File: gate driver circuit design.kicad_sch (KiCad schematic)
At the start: 105 parts, among them J101 90122-0763, J102 90121-0762, J103 90121-0762, Q1 CSD17313Q2, Q2 MMBT3904T-7-F, Q3 MMBT3904T-7-F, Q4 MMBT3904T-7-F, T1 750343725, T2 750343725, U1 SN6501QDBVRQ1, U2 TPS7B6950QDCYRQ1, U3 TL431AQDBZRQ1, U4 SN6501QDBVRQ1, U5 TL431AQDBZRQ1, U6 UCC21530QDWKRQ1, U7 ISO7721QDRQ1, U8 LMV762QMA_NOPB, U9 TL431AQDBZRQ1

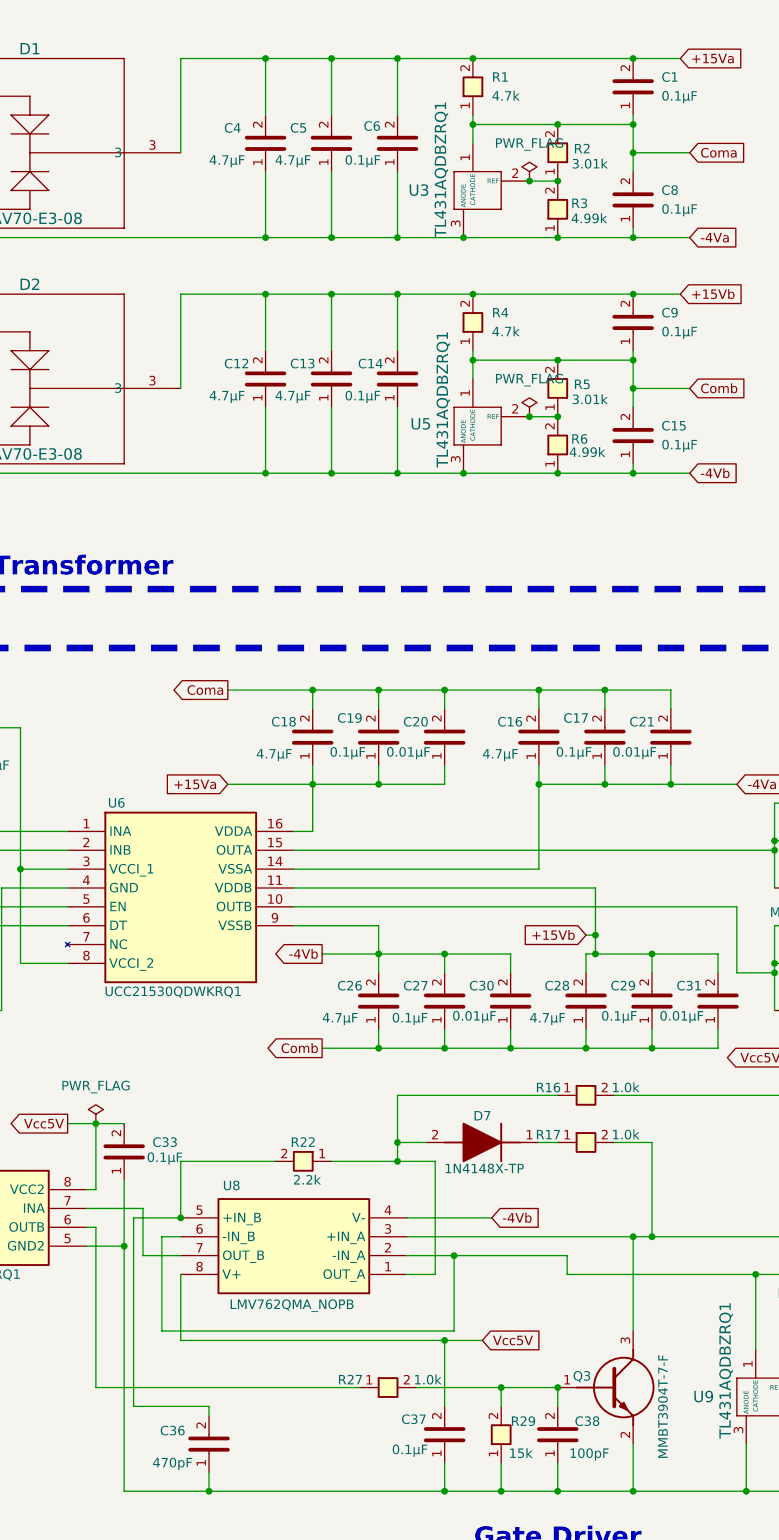
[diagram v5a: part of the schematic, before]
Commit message: Final PCB design TI gate driver
TI gate driver final PCB design files
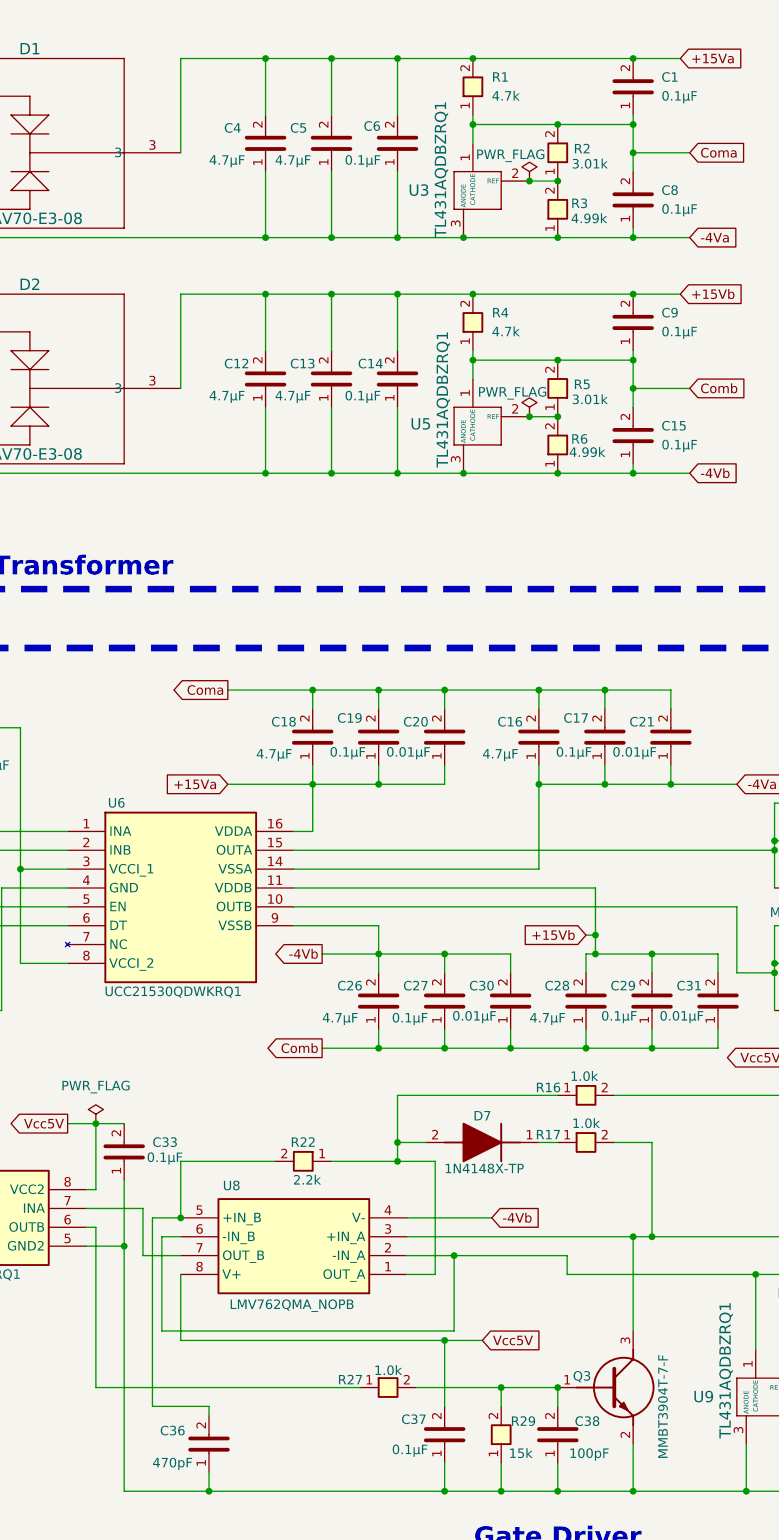
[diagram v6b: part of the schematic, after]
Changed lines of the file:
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@@
 	(wire
 		(pts
-			(xy 157.48 212.09) (xy 167.64 212.09)
+			(xy 160.02 212.09) (xy 167.64 212.09)
 		)
 		(stroke
@@
 	(wire
 		(pts
-			(xy 157.48 186.69) (xy 157.48 212.09)
+			(xy 160.02 186.69) (xy 160.02 212.09)
 		)
 		(stroke
@@
 	(wire
 		(pts
-			(xy 163.83 186.69) (xy 157.48 186.69)
+			(xy 163.83 186.69) (xy 160.02 186.69)
 		)
 		(stroke
@@
 		)
 		(property "Value" "1.0k"
-			(at 223.774 175.514 0)
+			(at 218.44 173.99 0)
 			(effects
 				(font
@@
 		)
 		(property "Value" "1.0k"
-			(at 197.104 208.534 0)
+			(at 191.77 207.264 0)
 			(effects
 				(font
@@
 		(on_board yes)
 		(dnp no)
-		(fields_autoplaced yes)
 		(property "Reference" "#FLG06"
 			(at 210.82 76.835 0)
@@
 		)
 		(property "Value" "PWR_FLAG"
-			(at 210.82 73.66 0)
+			(at 208.534 75.438 0)
 			(effects
 				(font
@@
 		)
 		(property "Value" "1.0k"
-			(at 223.774 169.164 0)
+			(at 218.186 167.64 0)
 			(effects
 				(font
@@
 		(on_board yes)
 		(dnp no)
-		(fields_autoplaced yes)
 		(property "Reference" "#FLG08"
 			(at 210.82 45.085 0)
@@
 		)
 		(property "Value" "PWR_FLAG"
-			(at 210.82 41.91 0)
+			(at 208.28 43.434 0)
 			(effects
 				(font
